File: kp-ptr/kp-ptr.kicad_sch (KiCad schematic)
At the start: 28 parts, among them J1 ANT1, U1 ESP32-S3FN8, Y1 7M40000005-40MHz

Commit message: Footprinty drobnicy
Signed-off-by: kretu <krecik@gmail.com>
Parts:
- C1, C10, C11, C12, C13, C14, C15, C16, C2, C3, C4, C5, C6, C7, C8, C9: footprint Capacitor_SMD:C_01005_0402Metric_Pad0.57x0.30mm_HandSolder -> Capacitor_SMD:C_0402_1005Metric_Pad0.74x0.62mm_HandSolder

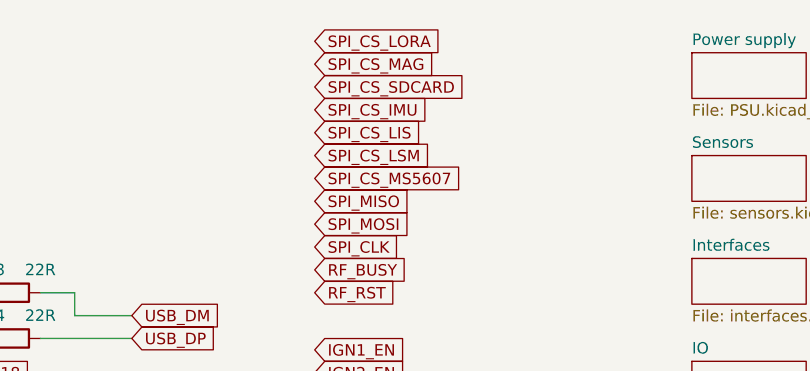
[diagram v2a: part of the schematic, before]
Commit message: Removed SD card
Added Flash
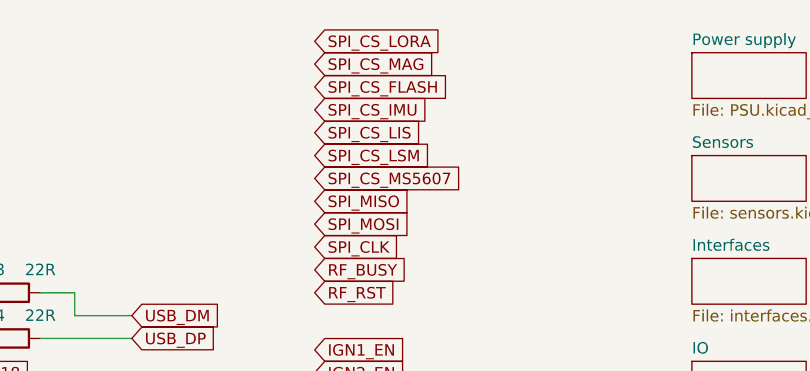
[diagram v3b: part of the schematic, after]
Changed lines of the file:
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@@
     )
   )
-  (global_label "SPI_CS_SDCARD" (shape input) (at 215.9 22.86 0) (fields_autoplaced)
+  (global_label "SPI_CS_FLASH" (shape input) (at 215.9 22.86 0) (fields_autoplaced)
     (effects (font (size 1.27 1.27)) (justify left))
-    (property "Intersheet References" "${INTERSHEET_REFS}" (id 0) (at 233.1902 22.9394 0)
+    (property "Intersheet References" "${INTERSHEET_REFS}" (id 0) (at 231.5574 22.7806 0)
       (effects (font (size 1.27 1.27)) (justify left) hide)
     )
@@
       (reference "#PWR0112") (unit 1) (value "Earth") (footprint "")
     )
-    (path "/5f9da060-2eb0-4ae6-ad5b-b0da419a62a6/d73cd4be-2523-4c44-8f7d-5b3e0b412f11"
-      (reference "#PWR0113") (unit 1) (value "+3.3V") (footprint "")
-    )
     (path "/5f9da060-2eb0-4ae6-ad5b-b0da419a62a6/8f206d15-b234-44d2-9f0b-5663775abcb3"
       (reference "#PWR0114") (unit 1) (value "VBUS") (footprint "")
@@
       (reference "#PWR0117") (unit 1) (value "Earth") (footprint "")
     )
-    (path "/5f9da060-2eb0-4ae6-ad5b-b0da419a62a6/3f2b9816-0353-4471-8753-8626d6dd2b30"
-      (reference "#PWR0118") (unit 1) (value "Earth") (footprint "")
-    )
     (path "/5f9da060-2eb0-4ae6-ad5b-b0da419a62a6/0dc485c2-a5e4-4981-b245-6e2aca26d21f"
       (reference "#PWR0119") (unit 1) (value "VBUS") (footprint "")
@@
       (reference "#PWR0161") (unit 1) (value "Earth") (footprint "")
     )
+    (path "/5f9da060-2eb0-4ae6-ad5b-b0da419a62a6/5559a045-e4ae-42f2-a983-31fb54c63da9"
+      (reference "#PWR?") (unit 1) (value "+3.3V") (footprint "")
+    )
+    (path "/5f9da060-2eb0-4ae6-ad5b-b0da419a62a6/6b45d24f-dc3b-4e4a-aa75-668025f5989d"
+      (reference "#PWR?") (unit 1) (value "+3.3V") (footprint "")
+    )
+    (path "/5f9da060-2eb0-4ae6-ad5b-b0da419a62a6/88bb3a86-9d99-4b69-8476-d2cb2933a1ca"
+      (reference "#PWR?") (unit 1) (value "+3.3V") (footprint "")
+    )
+    (path "/5f9da060-2eb0-4ae6-ad5b-b0da419a62a6/9209db1c-36ac-4b21-b8c5-6c41a553f73f"
+      (reference "#PWR?") (unit 1) (value "+3.3V") (footprint "")
+    )
+    (path "/5f9da060-2eb0-4ae6-ad5b-b0da419a62a6/c25c290e-f2ba-498e-9371-ee2273e0ad18"
+      (reference "#PWR?") (unit 1) (value "+3.3V") (footprint "")
+    )
+    (path "/5f9da060-2eb0-4ae6-ad5b-b0da419a62a6/c3ad7fed-d4ca-46f3-9b18-90164da4d23f"
+      (reference "#PWR?") (unit 1) (value "Earth") (footprint "")
+    )
+    (path "/5f9da060-2eb0-4ae6-ad5b-b0da419a62a6/ffd48dd1-45cf-4f09-a639-cd636b7d892b"
+      (reference "#PWR?") (unit 1) (value "Earth") (footprint "")
+    )
     (path "/5f9da060-2eb0-4ae6-ad5b-b0da419a62a6/911c9e40-8d0a-4a95-a324-f646d3493355"
       (reference "ANT1") (unit 1) (value "TBD") (footprint "Resistor_SMD:R_0402_1005Metric_Pad0.72x0.64mm_HandSolder")
@@
       (reference "C42") (unit 1) (value "TBD") (footprint "Capacitor_SMD:C_0402_1005Metric_Pad0.74x0.62mm_HandSolder")
     )
+    (path "/5f9da060-2eb0-4ae6-ad5b-b0da419a62a6/31f6475a-1e9b-4bda-a878-78b0931b557f"
+      (reference "C?") (unit 1) (value "1uF") (footprint "Capacitor_SMD:C_0402_1005Metric_Pad0.74x0.62mm_HandSolder")
+    )
     (path "/1d5e7912-4d51-4a4c-b45e-2695b4191d61/fe4aa8de-26af-4479-a4c3-8e9e7477e9d5"
       (reference "D1") (unit 1) (value "TBD") (footprint "")
@@
       (reference "F4") (unit 1) (value "500mA") (footprint "Fuse:Fuse_1206_3216Metric_Pad1.42x1.75mm_HandSolder")
     )
-    (path "/5f9da060-2eb0-4ae6-ad5b-b0da419a62a6/015e4123-b7c0-4c56-8648-d728a8b12037"
-      (reference "FB1") (unit 1) (value "TBD") (footprint "Resistor_SMD:R_0402_1005Metric_Pad0.72x0.64mm_HandSolder")
-    )
     (path "/5f9da060-2eb0-4ae6-ad5b-b0da419a62a6/82aae44a-c9ee-4277-9258-adb407e6a613"
       (reference "IC1") (unit 1) (value "E22-900M22S") (footprint "KP-PTR_lib:E22-900M22S")
@@
       (reference "J4") (unit 1) (value "USB_C_Receptacle_USB2.0") (footprint "KP-PTR_lib:217B-BC02")
     )
-    (path "/5f9da060-2eb0-4ae6-ad5b-b0da419a62a6/17c96f47-0016-4c9f-857d-3bc54b0121c5"
-      (reference "J5") (unit 1) (value "Micro_SD_Card_Det") (footprint "KP-PTR_lib:GCT_MEM2051-00-195-00-A")
-    )
     (path "/6b0b54eb-96fb-4a56-9d20-0b579f8bbc83/41ed2c25-0a33-432a-b218-19f5f06c4866"
       (reference "J6") (unit 1) (value "Conn_01x02") (footprint "TerminalBlock_TE-Connectivity:TerminalBlock_TE_282834-2_1x02_P2.54mm_Horizontal")
@@
       (reference "R33") (unit 1) (value "100k") (footprint "Resistor_SMD:R_0402_1005Metric_Pad0.72x0.64mm_HandSolder")
     )
-    (path "/5f9da060-2eb0-4ae6-ad5b-b0da419a62a6/9feeb532-0ec5-4f07-9c00-466d23e3de15"
-      (reference "R34") (unit 1) (value "100k") (footprint "Resistor_SMD:R_0402_1005Metric_Pad0.72x0.64mm_HandSolder")
-    )
-    (path "/5f9da060-2eb0-4ae6-ad5b-b0da419a62a6/d85bf6e6-947e-43f6-9327-20010284babd"
-      (reference "R35") (unit 1) (value "100k") (footprint "Resistor_SMD:R_0402_1005Metric_Pad0.72x0.64mm_HandSolder")
-    )
-    (path "/5f9da060-2eb0-4ae6-ad5b-b0da419a62a6/07496a18-a2c7-45e3-b4fe-9003d5feedce"
-      (reference "R36") (unit 1) (value "100k") (footprint "Resistor_SMD:R_0402_1005Metric_Pad0.72x0.64mm_HandSolder")
-    )
     (path "/68d9bec4-a8fa-482b-99d8-a42578238d37/8ffdbc98-c688-487b-bcfd-0655cc6eaf42"

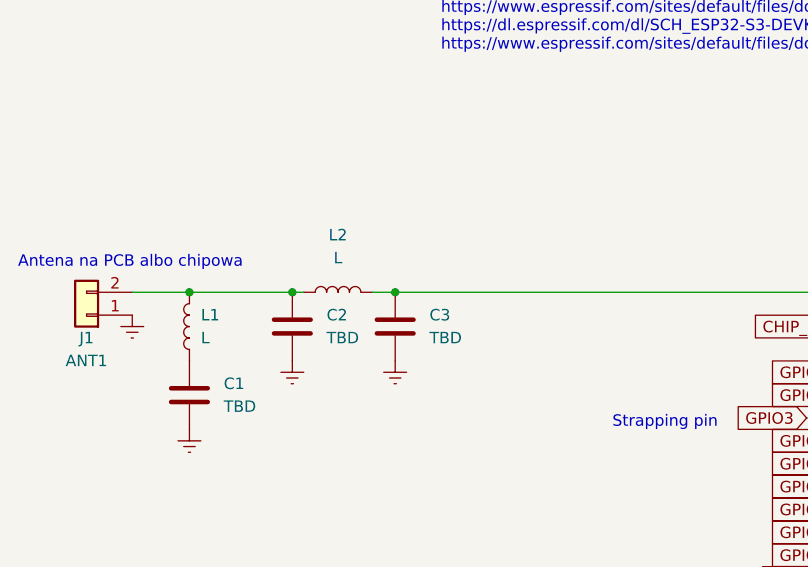
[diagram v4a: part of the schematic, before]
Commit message: Kilka zmian.
-dodany tranzystor P/N mosfet do biblioteki i zapalników
-dodany komentarz o impedancji ścieżek RF
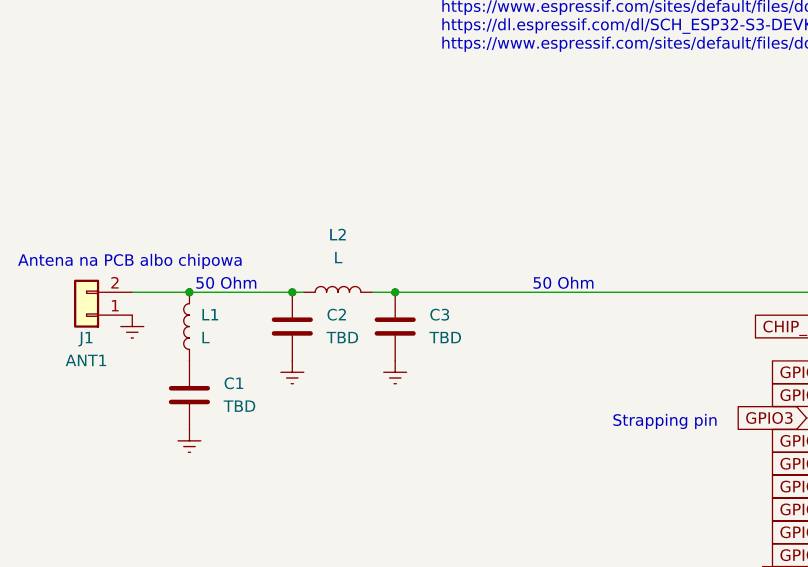
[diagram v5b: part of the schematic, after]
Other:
- note added: "50 Ohm"
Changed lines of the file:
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@@
+    (effects (font (size 1.27 1.27)) (justify left bottom))
+  )
+  (text "50 Ohm" (at 71.12 48.26 0)
     (effects (font (size 1.27 1.27)) (justify left bottom))
   )
@@
   )
   (text "Strapping pins" (at 207.01 97.79 0)
+    (effects (font (size 1.27 1.27)) (justify left bottom))
+  )
+  (text "50 Ohm" (at 33.655 48.26 0)
     (effects (font (size 1.27 1.27)) (justify left bottom))
   )
@@
       (reference "#PWR086") (unit 1) (value "Earth") (footprint "")
     )
-    (path "/f38dad53-0af4-40f6-a173-e0e37aecb5da/eddd775e-7791-4e5d-a8e1-b79926434229"
-      (reference "#PWR087") (unit 1) (value "VDD") (footprint "")
-    )
     (path "/f38dad53-0af4-40f6-a173-e0e37aecb5da/f467f7da-d51b-405e-8c73-d621186f5564"
       (reference "#PWR088") (unit 1) (value "Earth") (footprint "")
@@
       (reference "#PWR?") (unit 1) (value "Earth") (footprint "")
     )
+    (path "/f38dad53-0af4-40f6-a173-e0e37aecb5da/329592c8-62f7-4321-8672-477d4aa9e306"
+      (reference "#PWR?") (unit 1) (value "VBUS") (footprint "")
+    )
     (path "/1d5e7912-4d51-4a4c-b45e-2695b4191d61/34111a7c-e7fb-4663-a410-325d48633300"
       (reference "#PWR?") (unit 1) (value "+3.3V") (footprint "")
@@
       (reference "#PWR?") (unit 1) (value "+3.3V") (footprint "")
     )
+    (path "/f38dad53-0af4-40f6-a173-e0e37aecb5da/6c69ce45-7af5-406c-8c03-7e62d133f827"
+      (reference "#PWR?") (unit 1) (value "VCC") (footprint "")
+    )
     (path "/5f9da060-2eb0-4ae6-ad5b-b0da419a62a6/88bb3a86-9d99-4b69-8476-d2cb2933a1ca"
       (reference "#PWR?") (unit 1) (value "+3.3V") (footprint "")
@@
     )
     (path "/1d5e7912-4d51-4a4c-b45e-2695b4191d61/2b12b2d4-198b-4c76-b90a-d4d1638b8e72"
-      (reference "ANT?") (unit 1) (value "APAE1575R1340ABDD6-T") (footprint "")
+      (reference "ANT?") (unit 1) (value "APAE1575R1340ABDD6-T") (footprint "KP-PTR_lib:APAE1575 13x13x4mm GPS Patch Antenna")
     )
     (path "/b16fb66c-646a-4b14-8afd-faebe196e03a"
@@
       (reference "D10") (unit 1) (value "TBD") (footprint "")
     )
+    (path "/f38dad53-0af4-40f6-a173-e0e37aecb5da/55b5f7c1-9e27-4de8-8da9-4ddd7c634c2f"
+      (reference "D?") (unit 1) (value "D_Schottky") (footprint "Diode_SMD:D_SOD-123")
+    )
     (path "/1d5e7912-4d51-4a4c-b45e-2695b4191d61/c0e01ba5-ed56-4572-a513-e7708605b1ff"
       (reference "D?") (unit 1) (value "BLUE") (footprint "LED_SMD:LED_0603_1608Metric_Pad1.05x0.95mm_HandSolder")
@@
       (reference "Q5") (unit 1) (value "NMOS_SOT23") (footprint "Package_TO_SOT_SMD:SOT-23")
     )
-    (path "/6b0b54eb-96fb-4a56-9d20-0b579f8bbc83/1bea5378-7e85-4110-a5a2-db707671269e"
-      (reference "Q6") (unit 1) (value "NMOS_SOT23") (footprint "Package_TO_SOT_SMD:SOT-23")
-    )
-    (path "/6b0b54eb-96fb-4a56-9d20-0b579f8bbc83/90f662bd-9935-4cda-95a5-ab7729009125"
-      (reference "Q7") (unit 1) (value "NMOS_SOT23") (footprint "Package_TO_SOT_SMD:SOT-23")
-    )
-    (path "/6b0b54eb-96fb-4a56-9d20-0b579f8bbc83/12938643-23eb-459b-b3a7-66e54527f212"
-      (reference "Q8") (unit 1) (value "PMOS_SOT23") (footprint "Package_TO_SOT_SMD:SOT-23")
-    )
-    (path "/6b0b54eb-96fb-4a56-9d20-0b579f8bbc83/bc2610dd-e869-4057-93f0-45b98a83d316"
-      (reference "Q9") (unit 1) (value "PMOS_SOT23") (footprint "Package_TO_SOT_SMD:SOT-23")
-    )
-    (path "/6b0b54eb-96fb-4a56-9d20-0b579f8bbc83/95e0e249-315d-44ac-a64e-078d4a48dae2"
-      (reference "Q10") (unit 1) (value "NMOS_SOT23") (footprint "Package_TO_SOT_SMD:SOT-23")
-    )
-    (path "/6b0b54eb-96fb-4a56-9d20-0b579f8bbc83/1440c710-b7fd-4aac-af2a-747084d8fd9b"
-      (reference "Q11") (unit 1) (value "NMOS_SOT23") (footprint "Package_TO_SOT_SMD:SOT-23")
-    )
-    (path "/6b0b54eb-96fb-4a56-9d20-0b579f8bbc83/01ee9d6d-2280-4d04-b65a-b1536dfd4f7c"
-      (reference "Q12") (unit 1) (value "PMOS_SOT23") (footprint "Package_TO_SOT_SMD:SOT-23")
-    )
-    (path "/6b0b54eb-96fb-4a56-9d20-0b579f8bbc83/49907ab9-0e59-4f2c-9360-a9bd477707dd"
-      (reference "Q13") (unit 1) (value "PMOS_SOT23") (footprint "Package_TO_SOT_SMD:SOT-23")
+    (path "/6b0b54eb-96fb-4a56-9d20-0b579f8bbc83/8c4b64bb-e884-431d-bb9e-e94e6b868d84"
+      (reference "Q?") (unit 1) (value "DMC2025UFDB") (footprint "")
+    )
+    (path "/6b0b54eb-96fb-4a56-9d20-0b579f8bbc83/c33d0f7e-1fe6-4263-8371-03321a71eebc"
+      (reference "Q?") (unit 1) (value "DMC2025UFDB") (footprint "")
+    )
+    (path "/6b0b54eb-96fb-4a56-9d20-0b579f8bbc83/cf12cbe0-29c7-463b-9606-32f8fa4b7792"
+      (reference "Q?") (unit 1) (value "DMC2025UFDB") (footprint "")
+    )
+    (path "/6b0b54eb-96fb-4a56-9d20-0b579f8bbc83/f24d1059-63b1-479b-b1a4-76f6ef826da9"
+      (reference "Q?") (unit 1) (value "DMC2025UFDB") (footprint "")
+    )
+    (path "/6b0b54eb-96fb-4a56-9d20-0b579f8bbc83/1a38c62a-a590-4913-bbae-3d58dfdd375c"
+      (reference "Q?") (unit 2) (value "DMC2025UFDB") (footprint "")
+    )
+    (path "/6b0b54eb-96fb-4a56-9d20-0b579f8bbc83/2ea5f82f-738e-4788-bb70-93af997ad6ed"
+      (reference "Q?") (unit 2) (value "DMC2025UFDB") (footprint "")
+    )
+    (path "/6b0b54eb-96fb-4a56-9d20-0b579f8bbc83/357efaa5-6255-4fe0-9c6c-25aa8785237f"
+      (reference "Q?") (unit 2) (value "DMC2025UFDB") (footprint "")
+    )
+    (path "/6b0b54eb-96fb-4a56-9d20-0b579f8bbc83/8e9246da-73c4-4861-bfdf-953c9e5e05c5"
+      (reference "Q?") (unit 2) (value "DMC2025UFDB") (footprint "")
     )
     (path "/2c7c4624-5556-4f0a-9902-0e418133e1f8"

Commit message: Szlifowanie schematu
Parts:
- removed R6: 10k, Resistor_SMD:R_0402_1005Metric_Pad0.72x0.64mm_HandSolder, symbol Device:R
- added J?: ESP32_PROG_CON, symbol KP-PTR_lib:ESP32_PROG_CON
- added R? (x3): 1k, Resistor_SMD:R_0402_1005Metric_Pad0.72x0.64mm_HandSolder, symbol Device:R
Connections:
- net GPIO3 is gone; now on net RF_RST: U1.8 (GPIO3/ADC1_CH2)
- net GPIO46 is gone; now on net LED2: U1.52 (GPIO46)
- net +3V3: now also J?.1 (3V3)
- net BOOT_PIN: now also R2.1
- net BUZZER: now also U1.51 (GPIO45)
- net CHIP_PU: now also R?.1
- net Earth: now also J?.6 (GND)
- net GPIO42: now also U1.48 (MTMS/JTAG/GPIO42)
- net U0RXD: now also R?.1
- net U0TXD: now also U1.49 (U0TXD/PROG/GPIO43), R?.1; no longer R2.2
- new net: J?.5 (EN), R?.2
- new net: J?.4 (BOOT), R2.2
- new net: J?.2 (RX0), R?.2
- new net: J?.3 (TX0), R?.2
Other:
- note added: "Strapping pin | USB-JTAG = pullup"
- note added: "Strapping pins <-- nie zmieniać, bo będzie problem"
- note removed: "Strapping pins"
- moved on the sheet: R2

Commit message: Update po spotkaniu
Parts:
- removed C1: TBD, Capacitor_SMD:C_0402_1005Metric_Pad0.74x0.62mm_HandSolder, symbol Device:C
- removed J1: ANT1, symbol Connector_Generic:Conn_01x02
- removed L1: L, symbol Device:L
- added ANT2: PCB_antenna, RF_Antenna:Texas_SWRA117D_2.4GHz_Right, symbol Device:Antenna_Dipole
- C10, C11, C12, C13, C14, C15, C16, C4, C5, C6, C7: footprint Capacitor_SMD:C_0402_1005Metric_Pad0.74x0.62mm_HandSolder -> Capacitor_SMD:C_0402_1005Metric
- C2: value TBD -> 4pF; footprint Capacitor_SMD:C_0402_1005Metric_Pad0.74x0.62mm_HandSolder -> Capacitor_SMD:C_0402_1005Metric
- C3: value TBD -> 5pF; footprint Capacitor_SMD:C_0402_1005Metric_Pad0.74x0.62mm_HandSolder -> Capacitor_SMD:C_0402_1005Metric
- C8: value TBD -> 100n; footprint Capacitor_SMD:C_0402_1005Metric_Pad0.74x0.62mm_HandSolder -> Capacitor_SMD:C_0402_1005Metric
- C9: value 10u -> 10n; footprint Capacitor_SMD:C_0402_1005Metric_Pad0.74x0.62mm_HandSolder -> Capacitor_SMD:C_0402_1005Metric
- J1: renamed from J?; footprint (none) -> Connector_PinHeader_1.27mm:PinHeader_1x06_P1.27mm_Vertical
- L2: value L -> 1.8nH; footprint (none) -> Inductor_SMD:L_0402_1005Metric
- L3: value L -> 2nH; footprint (none) -> Inductor_SMD:L_0402_1005Metric
- R1, R2, R3, R4, R5: footprint Resistor_SMD:R_0402_1005Metric_Pad0.72x0.64mm_HandSolder -> Resistor_SMD:R_0402_1005Metric
- R14, R6, R8: renamed from R?; footprint Resistor_SMD:R_0402_1005Metric_Pad0.72x0.64mm_HandSolder -> Resistor_SMD:R_0402_1005Metric
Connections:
- net Earth: now also ANT2.2
- net at C2.1, L2.1: now also ANT2.1
- net VDD_SPI: no longer names the net of C13.1, C14.1, U1.29 (VDD_SPI)
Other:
- note removed: "Antena na PCB albo chipowa"
- note removed: "Nie wiem czy potrzebne jeśli mamy wewnętrzny FLASH"
- note removed: "To zasilania zrobię później po swojemu"
